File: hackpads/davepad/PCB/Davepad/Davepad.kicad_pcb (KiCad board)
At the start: 2 copper layers, 100 x 100 mm, 54 parts, among them J1 To OLED, SW1 SW_Push, SW10 SW_Push, SW11 SW_Push, SW12 SW_Push, SW13 RotaryEncoder_Switch, SW14 SW_Push, SW15 SW_Push, SW16 SW_Push, SW17 RotaryEncoder_Switch, SW18 SW_Push, SW19 SW_Push, SW2 SW_Push, SW20 SW_Push, SW3 SW_Push, SW4 SW_Push, SW5 SW_Push, SW6 SW_Push, SW7 SW_Push, SW8 SW_Push, SW9 SW_Push, U1 Seeed Studio XIAO SAMD21, U2 MCP23017_SP

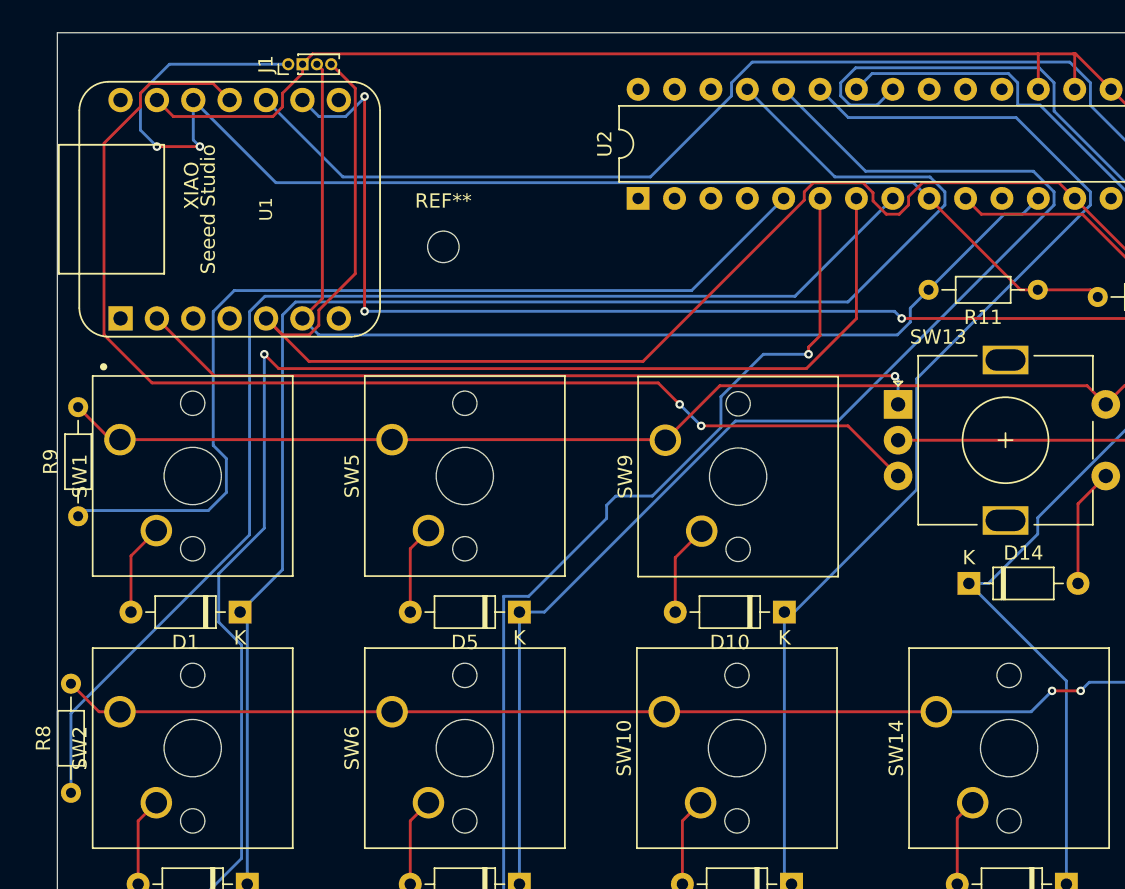
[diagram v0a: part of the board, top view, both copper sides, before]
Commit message: Add gerbers, change OLED footprint
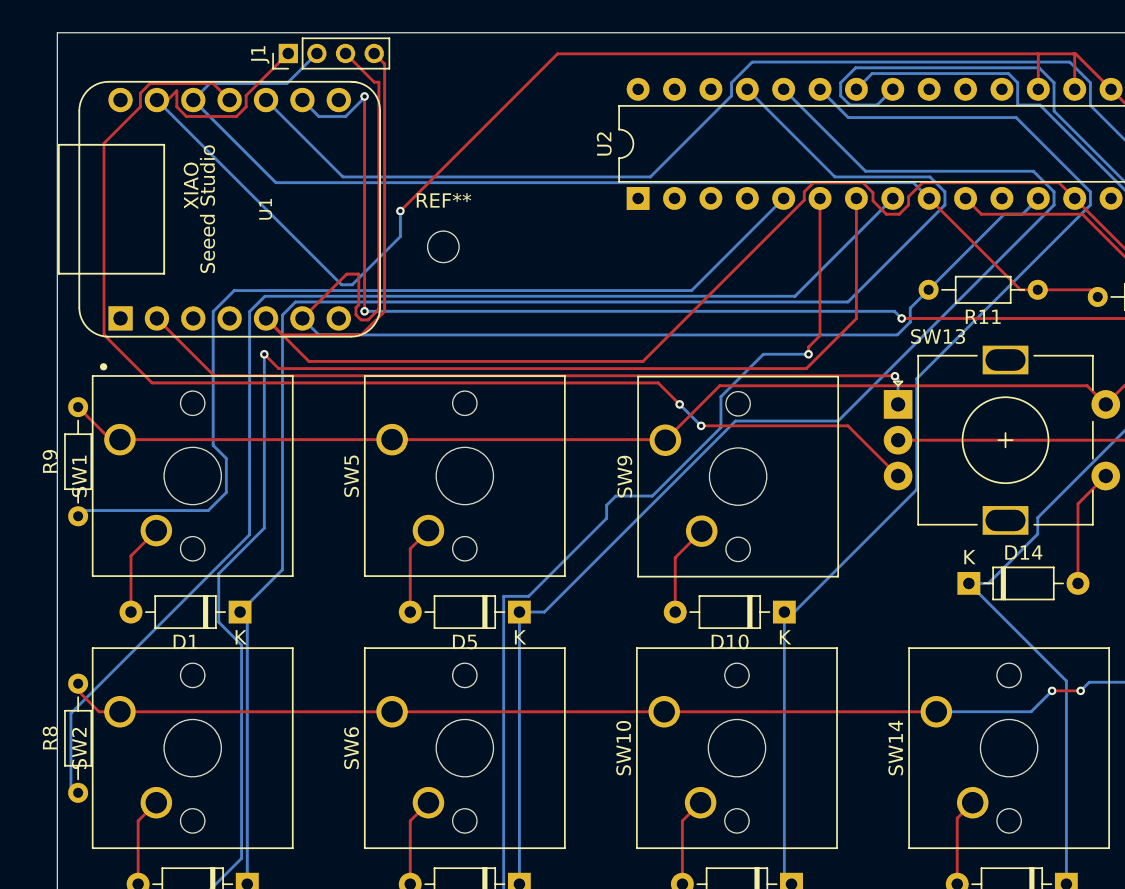
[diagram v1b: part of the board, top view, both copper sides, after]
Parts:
- J1: footprint Connector_PinHeader_1.00mm:PinHeader_1x04_P1.00mm_Vertical -> Connector_PinHeader_2.00mm:PinHeader_1x04_P2.00mm_Vertical
- moved J1 0.75 mm to (35.2, 20.5)
- moved R8 0.50 mm to (20.5, 72.1)
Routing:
- net GND: track 147.2 -> 170.2 mm, vias 1 -> 2
- net Net-(J1-Pin_2): track 90.6 -> 78.8 mm, vias 2 -> 0
- net SCL: track 74.9 -> 85.6 mm
- net SDA: track 102.7 -> 106.0 mm
- net Row1: track 67.1 -> 66.6 mm
